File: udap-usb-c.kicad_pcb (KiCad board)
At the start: 2 copper layers, 25 x 10 mm, 25 parts, among them J201 Conn_02x04_Counter_Clockwise, P1 USB_C_Plug, U2 MIC5245-3.3YM5, U201 NUF6401MNT1, U202 STM32F042F6Px, U4 NUF2042XV6T1G

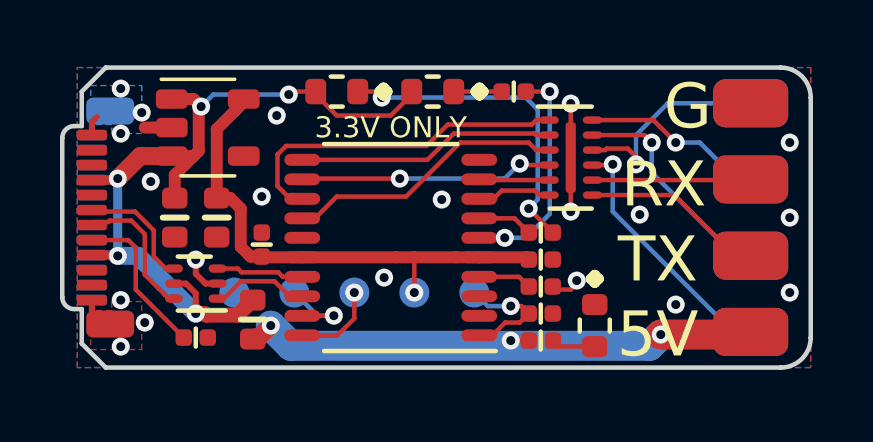
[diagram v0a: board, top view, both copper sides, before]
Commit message: Added ferrite bead on 5V, PC EMI -> TARGET issue mitigation
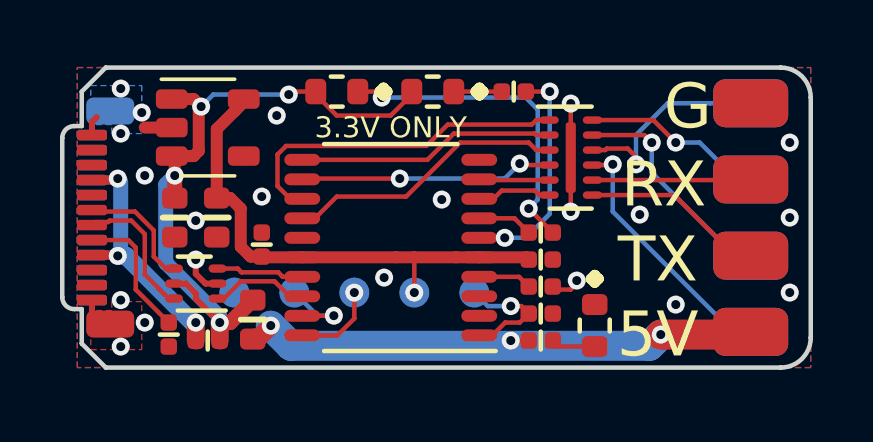
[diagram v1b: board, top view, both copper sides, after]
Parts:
- added FB101: Ferrite_Bead_Small, passive:R_0402, F.Cu at (94.4, 110.1)
- moved R3 0.91 mm to (93.1, 109.9), turned to 270 degrees
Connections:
- P1 pad A4: +5V -> Net-(FB101-Pad2)
- P1 pad A9: +5V -> Net-(FB101-Pad2)
- P1 pad B4: +5V -> Net-(FB101-Pad2)
- P1 pad B9: +5V -> Net-(FB101-Pad2)
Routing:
- net Net-(FB101-Pad2): track 0.00 -> 10.3 mm, vias 0 -> 3
- net +5V: track 28.2 -> 24.2 mm, vias 5 -> 4
- net Net-(P1-PadA5): track 5.23 -> 4.52 mm
- net GND: vias 20 -> 21
